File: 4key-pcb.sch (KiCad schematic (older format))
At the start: 24 parts

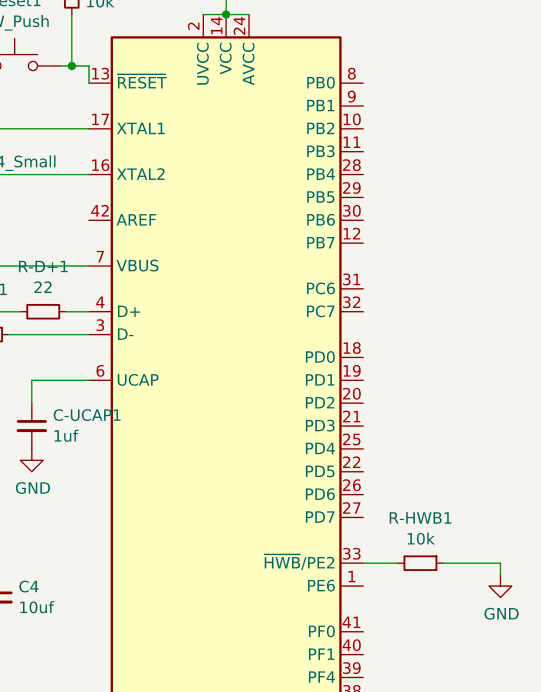
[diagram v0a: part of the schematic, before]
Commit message: finished routing mcu
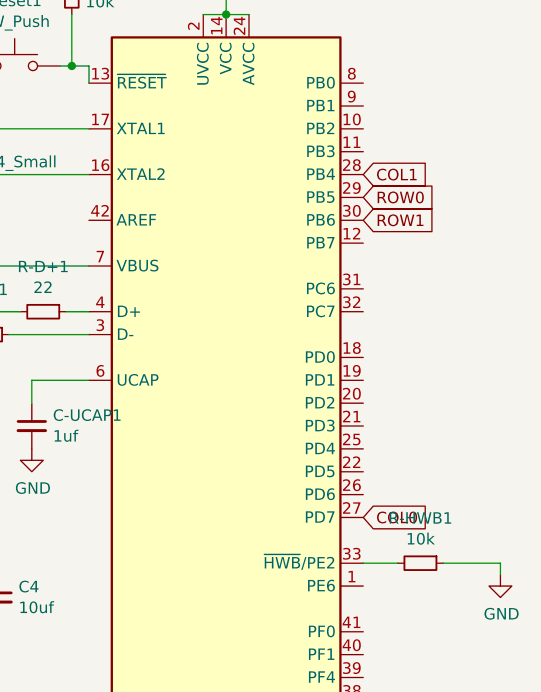
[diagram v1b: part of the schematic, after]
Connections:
- net COL0: now also MCU1.27 (PD7)
- net COL1: now also MCU1.28 (PB4)
- net ROW0: now also MCU1.29 (PB5)
- net ROW1: now also MCU1.30 (PB6)
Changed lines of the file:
@@
 Text GLabel 2225 1575 1    50   Input ~ 0
 COL1
+Text GLabel 9300 3650 2    50   Input ~ 0
+COL0
+Text GLabel 9300 2150 2    50   Input ~ 0
+COL1
+Text GLabel 9300 2250 2    50   Input ~ 0
+ROW0
+Text GLabel 9300 2350 2    50   Input ~ 0
+ROW1
 $EndSCHEMATC

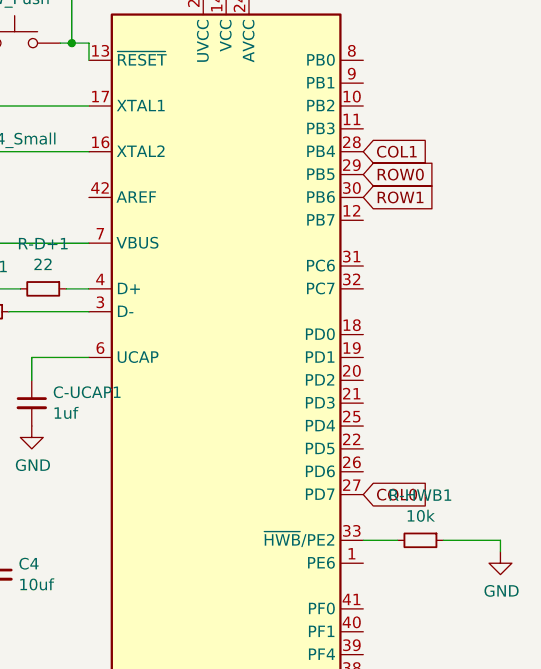
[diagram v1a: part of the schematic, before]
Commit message: finished pcb routing
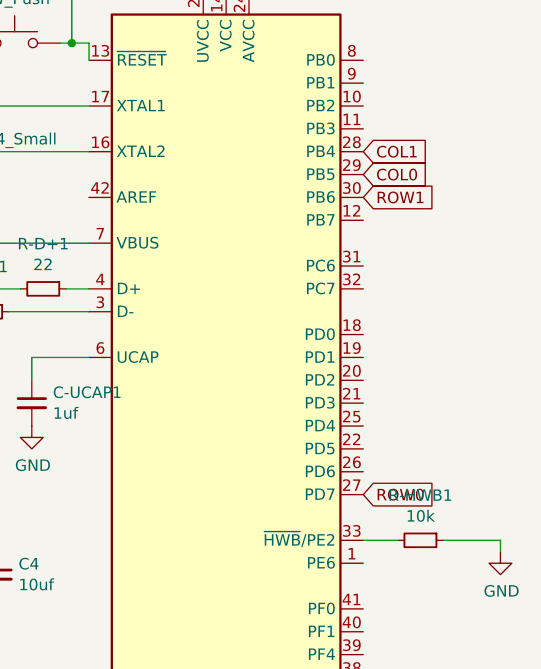
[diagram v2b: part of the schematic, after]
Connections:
- net COL0: now also MCU1.29 (PB5); no longer MCU1.27 (PD7)
- net ROW0: now also MCU1.27 (PD7); no longer MCU1.29 (PB5)
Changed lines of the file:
@@
 Text GLabel 2225 1575 1    50   Input ~ 0
 COL1
-Text GLabel 9300 3650 2    50   Input ~ 0
+Text GLabel 9300 2250 2    50   Input ~ 0
 COL0
 Text GLabel 9300 2150 2    50   Input ~ 0
 COL1
-Text GLabel 9300 2250 2    50   Input ~ 0
+Text GLabel 9300 3650 2    50   Input ~ 0
 ROW0
 Text GLabel 9300 2350 2    50   Input ~ 0

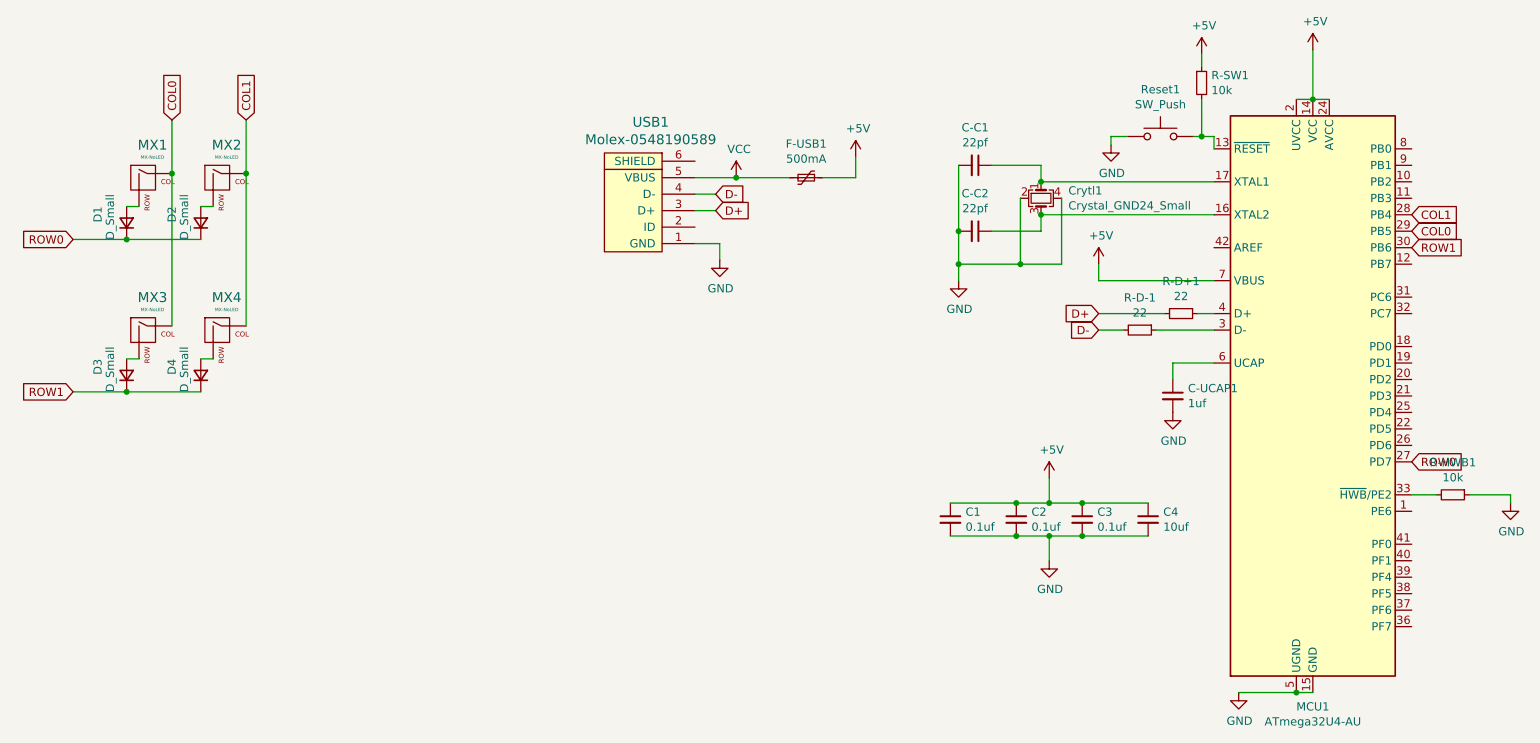
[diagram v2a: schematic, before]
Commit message: updated to usb-c
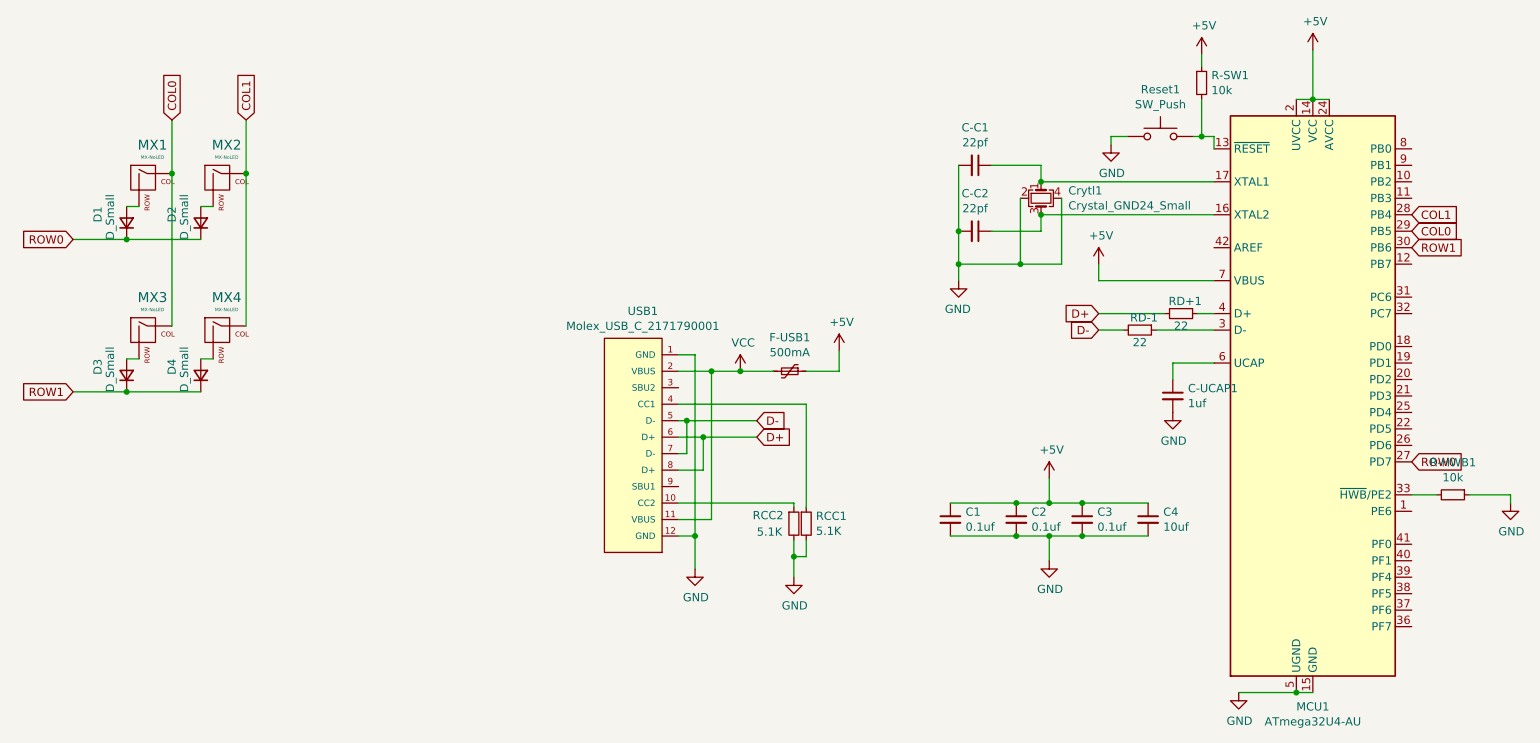
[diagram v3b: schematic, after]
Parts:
- removed USB1: Molex-0548190589, random-keyboard-parts:Molex-0548190589, symbol random-keyboard-parts:Molex-0548190589
- added RCC1, RCC2: 5.1K, Resistor_SMD:R_0805_2012Metric, symbol Device:R_Small
- added USB1: Molex_USB_C_2171790001, Connector_Molex:Molex_USB-C_2171790001, symbol Connector:Molex_USB_C_2171790001
- C-C1, C-C2, C-UCAP1, C2, C3, C4: footprint Capacitor_THT:C_Rect_L29.0mm_W13.8mm_P27.50mm_MKT -> Capacitor_SMD:C_0805_2012Metric
- C1: footprint Capacitor_THT:C_Rect_L29.0mm_W13.8mm_P27.50mm_MKT -> Capacitor_SMD:C_0805_2012Metric_Pad1.18x1.45mm_HandSolder
- renumbered R-D+1 to RD+1, R-D-1 to RD-1
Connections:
- net D+: now also USB1.6 (D+), USB1.8 (D+)
- net D-: now also USB1.5 (D-), USB1.7 (D-)
- net GND: now also RCC1.2, RCC2.2, USB1.1 (GND), USB1.12 (GND)
- net VCC: now also USB1.11 (VBUS), USB1.2 (VBUS)
- new net: RCC2.1, USB1.10 (CC2)
- new net: RCC1.1, USB1.4 (CC1)
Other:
- moved on the sheet: F-USB1
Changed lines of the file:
@@
 	9900 3850 9900 3900
 $Comp
-L Device:R_Small R-D+1
+L Device:R_Small RD+1
 U 1 1 5FDA6EA0
 P 7900 2750
-F 0 "R-D+1" V 7704 2750 50  0000 C CNN
-F 1 "22" V 7795 2750 50  0000 C CNN
+F 0 "RD+1" V 7825 2775 50  0000 C CNN
+F 1 "22" V 7975 2750 50  0000 C CNN
 F 2 "Resistor_SMD:R_0805_2012Metric" H 7900 2750 50  0001 C CNN
 F 3 "~" H 7900 2750 50  0001 C CNN
@@
 $EndComp
 $Comp
-L Device:R_Small R-D-1
+L Device:R_Small RD-1
 U 1 1 5FDA6F1E
 P 7650 2850
-F 0 "R-D-1" V 7454 2850 50  0000 C CNN
-F 1 "22" V 7545 2850 50  0000 C CNN
+F 0 "RD-1" V 7575 2875 50  0000 C CNN
+F 1 "22" V 7725 2850 50  0000 C CNN
 F 2 "Resistor_SMD:R_0805_2012Metric" H 7650 2850 50  0001 C CNN
 F 3 "~" H 7650 2850 50  0001 C CNN
@@
 F 0 "C-UCAP1" H 7942 3296 50  0000 L CNN
 F 1 "1uf" H 7942 3205 50  0000 L CNN
-F 2 "Capacitor_THT:C_Rect_L29.0mm_W13.8mm_P27.50mm_MKT" H 7850 3250 50  0001 C CNN
+F 2 "Capacitor_SMD:C_0805_2012Metric" H 7850 3250 50  0001 C CNN
 F 3 "~" H 7850 3250 50  0001 C CNN
 	1    7850 3250
@@
 F 0 "C1" H 6592 4046 50  0000 L CNN
 F 1 "0.1uf" H 6592 3955 50  0000 L CNN
-F 2 "Capacitor_THT:C_Rect_L29.0mm_W13.8mm_P27.50mm_MKT" H 6500 4000 50  0001 C CNN
+F 2 "Capacitor_SMD:C_0805_2012Metric_Pad1.18x1.45mm_HandSolder" H 6500 4000 50  0001 C CNN
 F 3 "~" H 6500 4000 50  0001 C CNN
 	1    6500 4000
@@
 F 0 "C2" H 6992 4046 50  0000 L CNN
 F 1 "0.1uf" H 6992 3955 50  0000 L CNN
-F 2 "Capacitor_THT:C_Rect_L29.0mm_W13.8mm_P27.50mm_MKT" H 6900 4000 50  0001 C CNN
+F 2 "Capacitor_SMD:C_0805_2012Metric" H 6900 4000 50  0001 C CNN
 F 3 "~" H 6900 4000 50  0001 C CNN
 	1    6900 4000
@@
 F 0 "C3" H 7392 4046 50  0000 L CNN
 F 1 "0.1uf" H 7392 3955 50  0000 L CNN
-F 2 "Capacitor_THT:C_Rect_L29.0mm_W13.8mm_P27.50mm_MKT" H 7300 4000 50  0001 C CNN
+F 2 "Capacitor_SMD:C_0805_2012Metric" H 7300 4000 50  0001 C CNN
 F 3 "~" H 7300 4000 50  0001 C CNN
 	1    7300 4000
@@
 F 0 "C4" H 7792 4046 50  0000 L CNN
 F 1 "10uf" H 7792 3955 50  0000 L CNN
-F 2 "Capacitor_THT:C_Rect_L29.0mm_W13.8mm_P27.50mm_MKT" H 7700 4000 50  0001 C CNN
+F 2 "Capacitor_SMD:C_0805_2012Metric" H 7700 4000 50  0001 C CNN
 F 3 "~" H 7700 4000 50  0001 C CNN
 	1    7700 4000
@@
 F 0 "C-C1" V 6421 1850 50  0000 C CNN
 F 1 "22pf" V 6512 1850 50  0000 C CNN
-F 2 "Capacitor_THT:C_Rect_L29.0mm_W13.8mm_P27.50mm_MKT" H 6650 1850 50  0001 C CNN
+F 2 "Capacitor_SMD:C_0805_2012Metric" H 6650 1850 50  0001 C CNN
 F 3 "~" H 6650 1850 50  0001 C CNN
 	1    6650 1850
@@
 F 0 "C-C2" V 6421 2250 50  0000 C CNN
 F 1 "22pf" V 6512 2250 50  0000 C CNN
-F 2 "Capacitor_THT:C_Rect_L29.0mm_W13.8mm_P27.50mm_MKT" H 6650 2250 50  0001 C CNN
+F 2 "Capacitor_SMD:C_0805_2012Metric" H 6650 2250 50  0001 C CNN
 F 3 "~" H 6650 2250 50  0001 C CNN
 	1    6650 2250
@@
 F 3 "" H 6550 2550 50  0001 C CNN
 	1    6550 2550
-	1    0    0    -1
+	-1   0    0    -1
 $EndComp
 Wire Wire Line
@@
 	7850 3050 8100 3050
 $Comp
-L random-keyboard-parts:Molex-0548190589 USB1
-U 1 1 5FDBCA81
-P 4650 2125
-F 0 "USB1" V 5187 2094 60  0000 C CNN
-F 1 "Molex-0548190589" V 5081 2094 60  0000 C CNN
-F 2 "random-keyboard-parts:Molex-0548190589" H 4650 2125 60  0001 C CNN
-F 3 "" H 4650 2125 60  0001 C CNN
-	1    4650 2125
-	0    -1   -1   0
-$EndComp
-$Comp
 L Device:Polyfuse_Small F-USB1
 U 1 1 5FDBCD7B
-P 5625 1925
-F 0 "F-USB1" V 5420 1925 50  0000 C CNN
-F 1 "500mA" V 5511 1925 50  0000 C CNN
-F 2 "Fuse:Fuse_1206_3216Metric" H 5675 1725 50  0001 L CNN
-F 3 "~" H 5625 1925 50  0001 C CNN
-	1    5625 1925
+P 5525 3100
+F 0 "F-USB1" V 5320 3100 50  0000 C CNN
+F 1 "500mA" V 5411 3100 50  0000 C CNN
+F 2 "Fuse:Fuse_1206_3216Metric" H 5575 2900 50  0001 L CNN
+F 3 "~" H 5525 3100 50  0001 C CNN
+	1    5525 3100
 	0    1    1    0
 $EndComp
-Wire Wire Line
-	4950 1925 5200 1925
 $Comp
 L power:+5V #PWR0111
 U 1 1 5FDBE695
-P 5925 1800
-F 0 "#PWR0111" H 5925 1650 50  0001 C CNN
-F 1 "+5V" H 5940 1973 50  0000 C CNN
-F 2 "" H 5925 1800 50  0001 C CNN
-F 3 "" H 5925 1800 50  0001 C CNN
-	1    5925 1800
-	1    0    0    -1
-$EndComp
-Wire Wire Line
-	5725 1925 5925 1925
-Wire Wire Line
-	5925 1925 5925 1800
+P 5825 2975
+F 0 "#PWR0111" H 5825 2825 50  0001 C CNN
+F 1 "+5V" H 5840 3148 50  0000 C CNN
+F 2 "" H 5825 2975 50  0001 C CNN
+F 3 "" H 5825 2975 50  0001 C CNN
+	1    5825 2975
+	1    0    0    -1
+$EndComp
+Wire Wire Line
+	5625 3100 5825 3100
+Wire Wire Line
+	5825 3100 5825 2975
 $Comp
 L power:VCC #PWR0112
 U 1 1 5FDBF375
-P 5200 1925
-F 0 "#PWR0112" H 5200 1775 50  0001 C CNN
-F 1 "VCC" H 5217 2098 50  0000 C CNN
-F 2 "" H 5200 1925 50  0001 C CNN
-F 3 "" H 5200 1925 50  0001 C CNN
-	1    5200 1925
-	1    0    0    -1
-$EndComp
-Connection ~ 5200 1925
-Wire Wire Line
-	5200 1925 5525 1925
-Text GLabel 5075 2125 2    50   Input ~ 0
+P 5225 3100
+F 0 "#PWR0112" H 5225 2950 50  0001 C CNN
+F 1 "VCC" H 5242 3273 50  0000 C CNN
+F 2 "" H 5225 3100 50  0001 C CNN
+F 3 "" H 5225 3100 50  0001 C CNN
+	1    5225 3100
+	1    0    0    -1
+$EndComp
+Text GLabel 5325 3500 2    50   Input ~ 0
 D+
-Text GLabel 5075 2025 2    50   Input ~ 0
+Text GLabel 5325 3400 2    50   Input ~ 0
 D-
-Wire Wire Line
-	5075 2125 4950 2125
-Wire Wire Line
-	5075 2025 4950 2025
-$Comp
-L power:GND #PWR0113
-U 1 1 5FDC2A67
-P 5100 2425
-F 0 "#PWR0113" H 5100 2175 50  0001 C CNN
-F 1 "GND" H 5105 2252 50  0000 C CNN
-F 2 "" H 5100 2425 50  0001 C CNN
-F 3 "" H 5100 2425 50  0001 C CNN
-	1    5100 2425
-	1    0    0    -1
-$EndComp
-Wire Wire Line
-	4950 2325 5100 2325
-Wire Wire Line
-	5100 2325 5100 2425
 $Comp
 L MX_Alps_Hybrid:MX-NoLED MX1
@@
 Text GLabel 9300 2350 2    50   Input ~ 0
 ROW1
+$Comp
+L Connector:Molex_USB_C_2171790001 USB1
+U 1 1 60FEE1CB
+P 4550 3500
+F 0 "USB1" H 4633 4265 50  0000 C CNN
+F 1 "Molex_USB_C_2171790001" H 4633 4174 50  0000 C CNN
+F 2 "Connector_Molex:Molex_USB-C_2171790001" H 4600 5000 50  0001 C CNN
+F 3 "" H 4850 4400 50  0001 C CNN
+	1    4550 3500
+	1    0    0    -1
+$EndComp
+Wire Wire Line
+	4850 3000 4950 3000
+Wire Wire Line
+	4950 3000 4950 4100
+Wire Wire Line
+	4950 4100 4850 4100
+$Comp
+L power:GND #PWR0113
+U 1 1 60FF7A13
+P 4950 4300
+F 0 "#PWR0113" H 4950 4050 50  0001 C CNN
+F 1 "GND" H 4955 4127 50  0000 C CNN
+F 2 "" H 4950 4300 50  0001 C CNN
+F 3 "" H 4950 4300 50  0001 C CNN
+	1    4950 4300
+	1    0    0    -1
+$EndComp
+Wire Wire Line
+	4950 4300 4950 4100
+Connection ~ 4950 4100
+Wire Wire Line
+	4850 4000 5050 4000
+Wire Wire Line
+	5050 4000 5050 3100
+Wire Wire Line
+	5050 3100 4850 3100
+Connection ~ 5050 3100
+Wire Wire Line
+	5425 3100 5225 3100
+Wire Wire Line
+	4850 3400 4900 3400
+Wire Wire Line
+	4850 3600 4900 3600
+Wire Wire Line
+	4900 3600 4900 3400
+Connection ~ 4900 3400
+Wire Wire Line
+	4900 3400 5325 3400
+Wire Wire Line
+	4850 3500 5000 3500
+Wire Wire Line
+	4850 3700 5000 3700
+Wire Wire Line
+	5000 3700 5000 3500
+Connection ~ 5000 3500
+Wire Wire Line
+	5000 3500 5325 3500
+Connection ~ 5225 3100
+Wire Wire Line
+	5225 3100 5050 3100
+$Comp
+L power:GND #PWR0114
+U 1 1 61039AF5
+P 5550 4350
+F 0 "#PWR0114" H 5550 4100 50  0001 C CNN
+F 1 "GND" H 5555 4177 50  0000 C CNN
+F 2 "" H 5550 4350 50  0001 C CNN
+F 3 "" H 5550 4350 50  0001 C CNN
+	1    5550 4350
+	1    0    0    -1
+$EndComp
+$Comp
+L Device:R_Small RCC1
+U 1 1 61042766
+P 5625 4025
+F 0 "RCC1" H 5684 4071 50  0000 L CNN
+F 1 "5.1K" H 5684 3980 50  0000 L CNN
+F 2 "Resistor_SMD:R_0805_2012Metric" H 5625 4025 50  0001 C CNN
+F 3 "~" H 5625 4025 50  0001 C CNN
+	1    5625 4025
+	1    0    0    -1
+$EndComp
+$Comp
+L Device:R_Small RCC2
+U 1 1 6104412D
+P 5550 4025
+F 0 "RCC2" H 5300 4075 50  0000 L CNN
+F 1 "5.1K" H 5325 3975 50  0000 L CNN
+F 2 "Resistor_SMD:R_0805_2012Metric" H 5550 4025 50  0001 C CNN
+F 3 "~" H 5550 4025 50  0001 C CNN
+	1    5550 4025
+	1    0    0    -1
+$EndComp
+Wire Wire Line
+	5550 3900 5550 3925
+Wire Wire Line
+	4850 3900 5550 3900
+Wire Wire Line
+	4850 3300 5625 3300
+Wire Wire Line
+	5625 3300 5625 3925
+Wire Wire Line
+	5625 4125 5625 4225
+Wire Wire Line
+	5625 4225 5550 4225
+Wire Wire Line
+	5550 4225 5550 4350
+Wire Wire Line
+	5550 4125 5550 4225
+Connection ~ 5550 4225
 $EndSCHEMATC
